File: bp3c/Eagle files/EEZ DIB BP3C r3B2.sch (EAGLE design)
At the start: 58 parts, among them IC1 TCA9534PWR, Q1 2N7002, Q2 2N7002, Q3 2N7002, Q4 2N7002, X1 ZL202-20G, X2 ZL202-20G, X3 ZL202-20G, X4 DS1022-2*20RF11, X5 DS1023-2*14S21, X6 DS1023-2*14S21, X7 DS1023-2*14S21, X8 N.C.

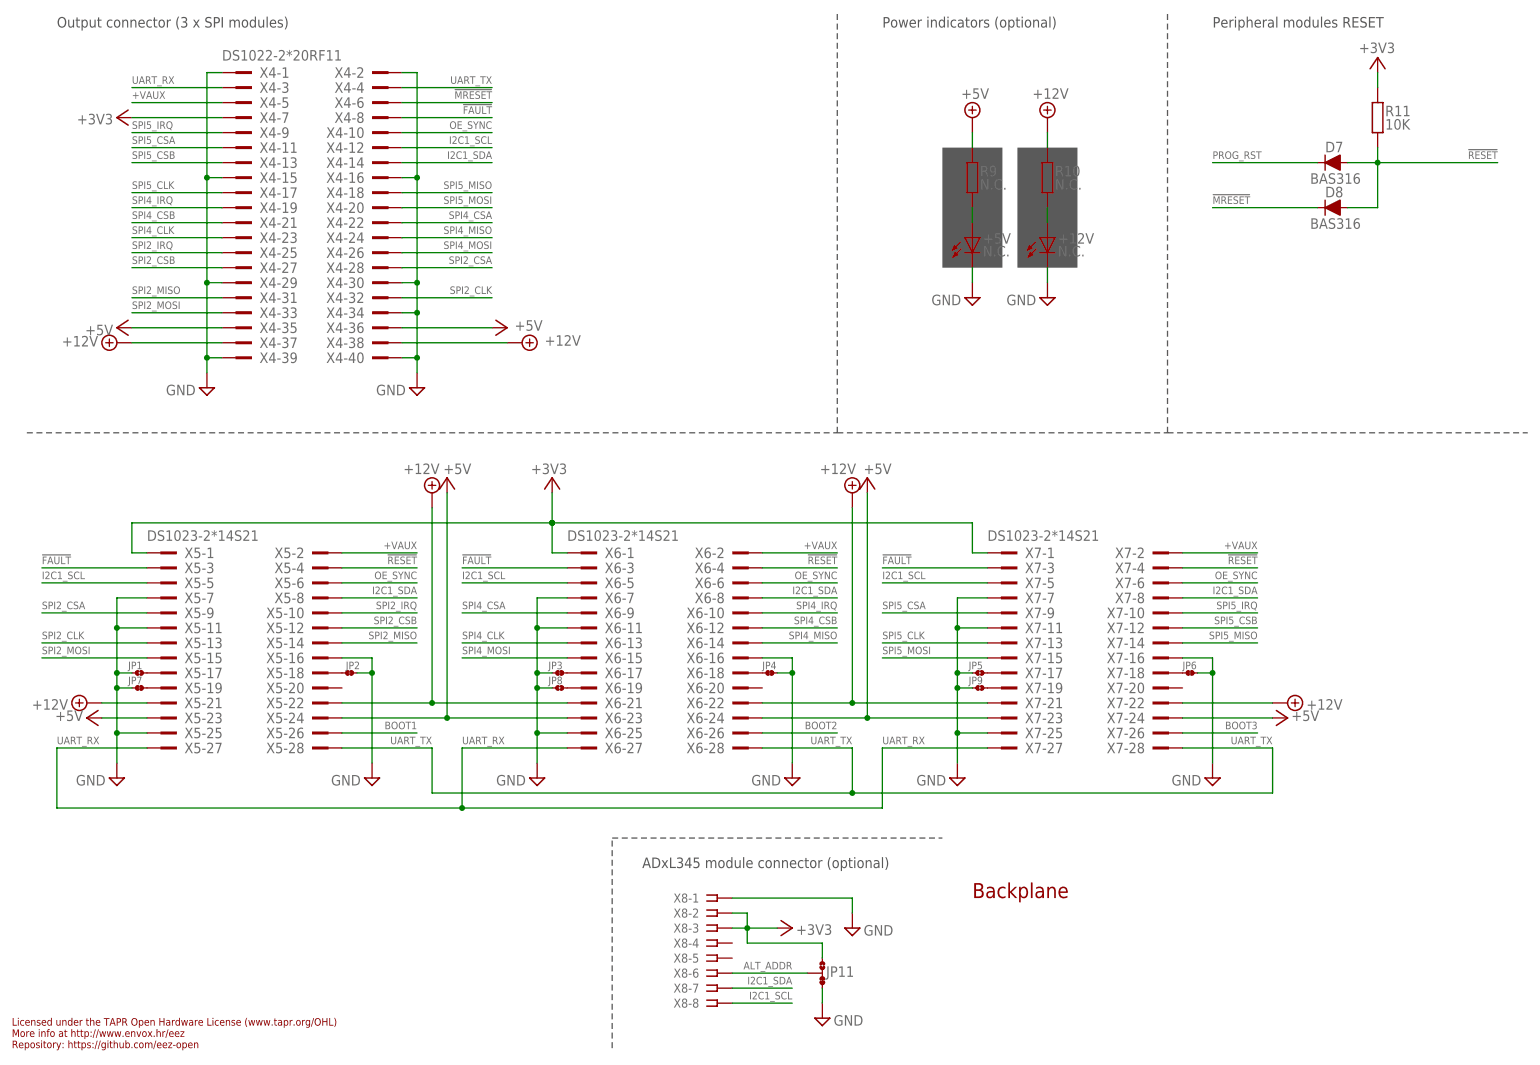
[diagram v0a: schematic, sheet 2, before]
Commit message: BP3C reset fix
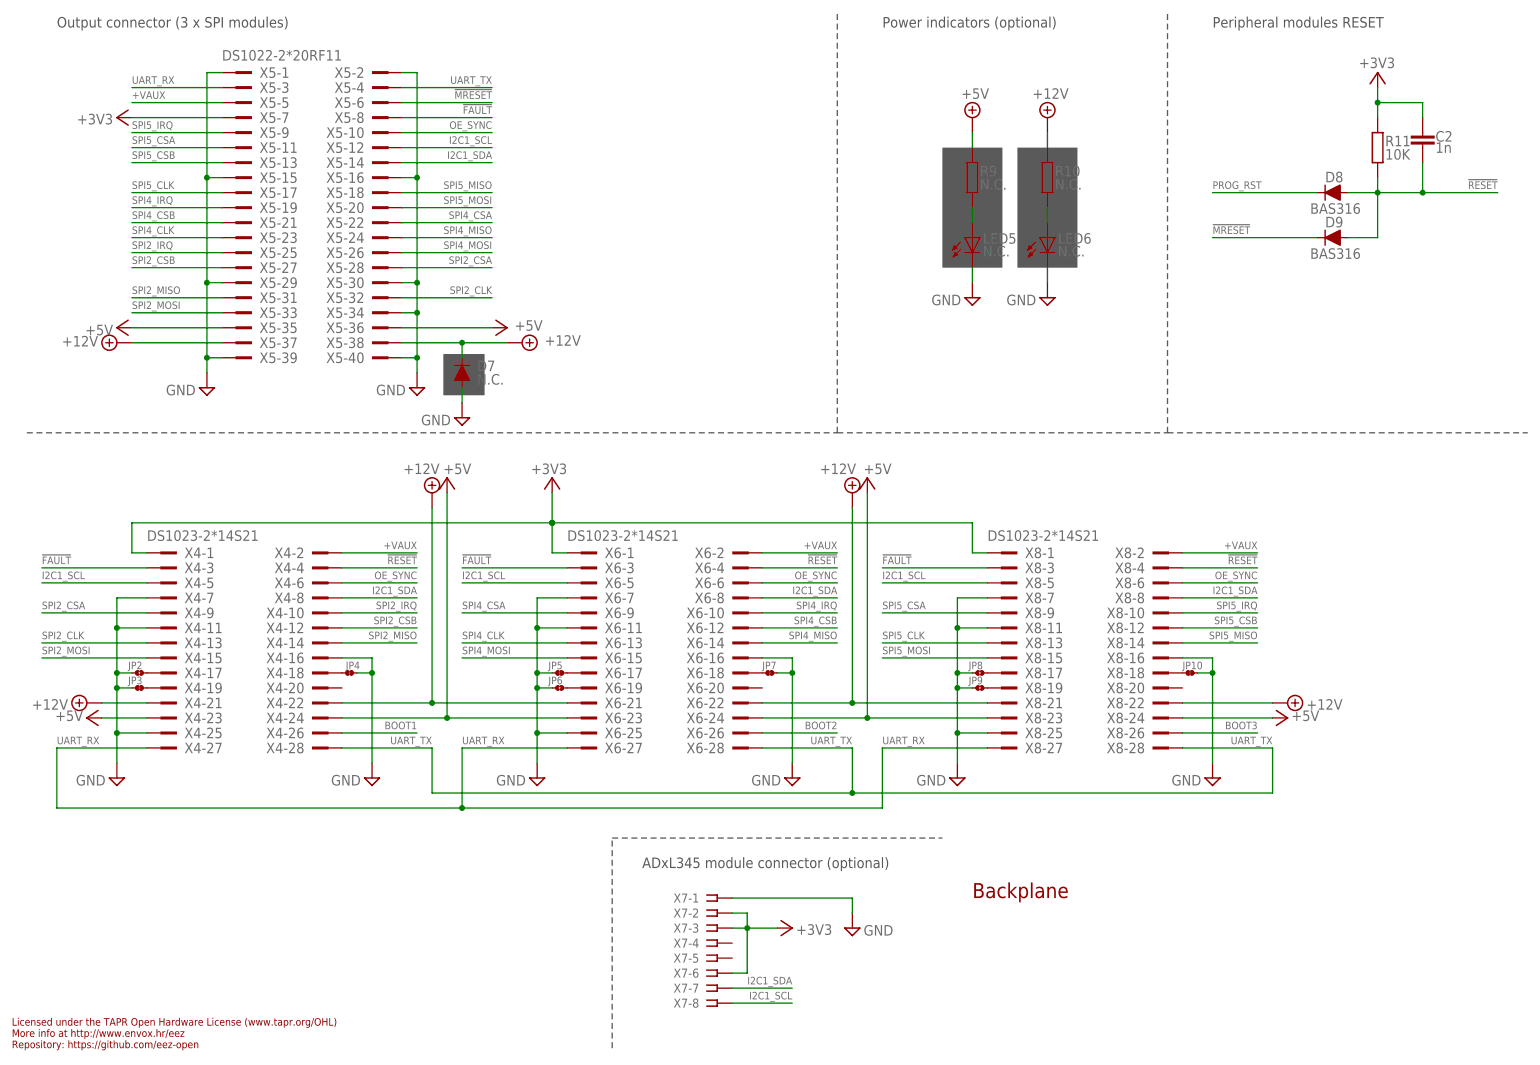
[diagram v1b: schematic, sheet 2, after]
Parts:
- removed JP11: JP3-CUT, EEZ_Lib1:JP3-CUT
- added C2: 1n, rcl:C-EUC0805
- added D9: BAS316, EEZ_Lib1:DIODESOD323R
- D1, D2: value BAS316 -> N.C.
- D3, D4: value N.C. -> BAS316
- D7: value BAS316 -> N.C.; device EEZ_Lib1:DIODESOD323R -> MyLib6:DIODEDO214AA
- JP1: value JP2-CUT -> JP3-CUT; device EEZ_Lib1:JP2-CUT -> EEZ_Lib1:JP3-CUT
- JP10: value JP3-CUT -> JP2-NOCUT; device EEZ_Lib1:JP3-CUT -> EEZ_Lib1:JP2-NOCUT
- JP2, JP6: value JP2-NOCUT -> JP2-CUT; device EEZ_Lib1:JP2-NOCUT -> EEZ_Lib1:JP2-CUT
- JP5: value JP2-CUT -> JP2-NOCUT; device EEZ_Lib1:JP2-CUT -> EEZ_Lib1:JP2-NOCUT
- R1, R5: value N.C. -> 100K
- R6, R8: value 100K -> N.C.
- X4: value DS1022-2*20RF11 -> DS1023-2*14S21; device EEZ_connectors:ZL212-40KG -> EEZ_connectors:TSW-114-07-F-D
- X5: value DS1023-2*14S21 -> DS1022-2*20RF11; device EEZ_connectors:TSW-114-07-F-D -> EEZ_connectors:ZL212-40KG
- X7: value DS1023-2*14S21 -> N.C.; device EEZ_connectors:TSW-114-07-F-D -> con-samtec:SSW-108-02-S-S
- X8: value N.C. -> DS1023-2*14S21; device con-samtec:SSW-108-02-S-S -> EEZ_connectors:TSW-114-07-F-D
- renumbered +12V to LED6, +5V to LED5, CGND to LED1, K_COMM to K3, K_PAR to K2, K_SER to K1, K_SRAIL to K4, PAR to LED2, SER to LED3, SRAIL to LED4
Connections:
- removed net ALT_ADDR: JP11.COM, X8-6.1
- removed net N$128 (its old number): D2.A, ZD2.A
- new net N$104: D4.A, ZD2.A
- net !FAULT: now also X4-3.1, X5-8.1, X8-3.1; no longer X4-8.1, X5-3.1, X7-3.1
- net !MRESET: now also D9.C, X5-6.1; no longer D8.C, X4-6.1
- net !RESET: now also C2.1, D9.A, X4-4.1, X8-4.1; no longer D7.A, X5-4.1, X7-4.1
- net +12V: now also D7.C, X4-21.1, X4-22.1, X5-37.1, X5-38.1, X8-21.1, X8-22.1; no longer X4-37.1, X4-38.1, X5-21.1, X5-22.1, X7-21.1, X7-22.1
- net +3V3: now also C2.2, JP1.NO, X4-1.1, X5-7.1, X7-2.1, X7-3.1, X7-6.1, X8-1.1; no longer JP10.NO, JP11.NO, X4-7.1, X5-1.1, X7-1.1, X8-2.1, X8-3.1
- net +5V: now also D3.C, D4.C, X4-23.1, X4-24.1, X5-35.1, X5-36.1, X8-23.1, X8-24.1; no longer D1.C, D2.C, X4-35.1, X4-36.1, X5-23.1, X5-24.1, X7-23.1, X7-24.1
- net +VAUX: now also X4-2.1, X5-5.1, X8-2.1; no longer X4-5.1, X5-2.1, X7-2.1
- net BOOT1: now also X4-26.1; no longer X5-26.1
- net BOOT3: now also X8-26.1; no longer X7-26.1
- net GND: now also D7.A, JP1.NC, JP10.2, JP2.1, JP6.1, JP7.2, R1.1, R5.1, X4-11.1, X4-25.1, X4-7.1, X5-1.1, X5-15.1, X5-2.1, X5-29.1, X5-30.1, X5-34.1, X5-39.1, X5-40.1, X7-1.1, X8-11.1, X8-16.1, X8-25.1, X8-7.1; no longer JP1.1, JP10.NC, JP11.NC, JP2.2, JP6.2, JP7.1, R6.1, R8.1, X4-1.1, X4-15.1, X4-2.1, X4-29.1, X4-30.1, X4-34.1, X4-39.1, X4-40.1, X5-11.1, X5-25.1, X5-7.1, X7-11.1, X7-16.1, X7-25.1, X7-7.1, X8-1.1
- net I2C1_SCL: now also X4-5.1, X5-12.1, X7-8.1, X8-5.1; no longer X4-12.1, X5-5.1, X7-5.1, X8-8.1
- net I2C1_SDA: now also X4-8.1, X5-14.1, X7-7.1, X8-8.1; no longer X4-14.1, X5-8.1, X7-8.1, X8-7.1
- net N$10: now also JP5.2; no longer JP3.2
- net N$101: now also Q2.D, R6.2, ZD2.C; no longer Q3.D, R5.2, ZD3.C
- net N$102: now also Q3.D, R7.2, ZD3.C; no longer Q2.D, R3.2, ZD2.C
- net N$11: now also JP6.2; no longer JP8.2
- net N$12: now also JP10.1, X8-18.1; no longer JP6.1, X7-18.1
- net N$13: now also JP8.2, X8-17.1; no longer JP5.2, X7-17.1
- net N$14: now also X8-19.1; no longer X7-19.1
- net N$15: now also JP1.COM; no longer JP10.COM
- net N$17: now also R3.2; no longer R1.2
- net N$18: now also D3.A; no longer D1.A
- net N$19: now also R3.1; no longer R1.1
- net N$2: now also JP4.1, X4-18.1; no longer JP2.1, X5-18.1
- net N$20: now also R8.2; no longer R7.2
- net N$22: now also R8.1; no longer R7.1
- net N$5: now also JP2.2, X4-17.1; no longer JP1.2, X5-17.1
- net N$6: now also JP3.2, X4-19.1; no longer JP7.2, X5-19.1
- net N$7: now also R6.1; no longer R5.1
- net N$8: now also R7.1; no longer R3.1
- net N$9: now also JP7.1; no longer JP4.1
- net OE_SYNC: now also X4-6.1, X5-10.1, X8-6.1; no longer X4-10.1, X5-6.1, X7-6.1
- net OUT_CGND: now also D1.C, R1.2; no longer D3.C, R2.2
- net OUT_PAR: now also D2.A, Q3.G; no longer D4.A, Q2.G
- net OUT_SER: now also D1.A, D2.C, Q2.G, R2.2; no longer D3.A, D4.C, Q3.G, R6.2
- net OUT_SRA: now also R5.2; no longer R8.2
- net PROG_RST: now also D8.C; no longer D7.C
- net SPI2_CLK: now also X4-13.1, X5-32.1; no longer X4-32.1, X5-13.1
- net SPI2_CSA: now also X4-9.1, X5-28.1; no longer X4-28.1, X5-9.1
- net SPI2_CSB: now also X4-12.1, X5-27.1; no longer X4-27.1, X5-12.1
- net SPI2_IRQ: now also X4-10.1, X5-25.1; no longer X4-25.1, X5-10.1
- net SPI2_MISO: now also X4-14.1, X5-31.1; no longer X4-31.1, X5-14.1
- net SPI2_MOSI: now also X4-15.1, X5-33.1; no longer X4-33.1, X5-15.1
- net SPI4_CLK: now also X5-23.1; no longer X4-23.1
- net SPI4_CSA: now also X5-22.1; no longer X4-22.1
- net SPI4_CSB: now also X5-21.1; no longer X4-21.1
- net SPI4_IRQ: now also X5-19.1; no longer X4-19.1
- net SPI4_MISO: now also X5-24.1; no longer X4-24.1
- net SPI4_MOSI: now also X5-26.1; no longer X4-26.1
- net SPI5_CLK: now also X5-17.1, X8-13.1; no longer X4-17.1, X7-13.1
- net SPI5_CSA: now also X5-11.1, X8-9.1; no longer X4-11.1, X7-9.1
- net SPI5_CSB: now also X5-13.1, X8-12.1; no longer X4-13.1, X7-12.1
- net SPI5_IRQ: now also X5-9.1, X8-10.1; no longer X4-9.1, X7-10.1
- net SPI5_MISO: now also X5-18.1, X8-14.1; no longer X4-18.1, X7-14.1
- net SPI5_MOSI: now also X5-20.1, X8-15.1; no longer X4-20.1, X7-15.1
- net UART_RX: now also X4-27.1, X5-3.1, X8-27.1; no longer X4-3.1, X5-27.1, X7-27.1
- net UART_TX: now also X4-28.1, X5-4.1, X8-28.1; no longer X4-4.1, X5-28.1, X7-28.1
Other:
- moved on the sheet: D1, D2, D3, D4, D5, D7, D8, JP3, JP4, JP7, JP8, Q2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

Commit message: add OSHWA ID on BP3C PCB
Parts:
- added OSHWA: HR000002, EEZ_Lib1:OSHWA-CERT-SMALL
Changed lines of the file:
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@@
 <setting verticaltext="up"/>
 </settings>
-<grid distance="0.1" unitdist="inch" unit="inch" style="lines" multiple="1" display="no" altdistance="0.01" altunitdist="inch" altunit="inch"/>
+<grid distance="0.025" unitdist="inch" unit="inch" style="lines" multiple="4" display="no" altdistance="0.01" altunitdist="inch" altunit="inch"/>
 <layers>
 <layer number="1" name="Top" color="4" fill="1" visible="no" active="no"/>
@@
 <part name="D7" library="MyLib6" deviceset="DIODE" device="DO214AA" value="N.C."/>
 <part name="SUPPLY14" library="supply2" deviceset="GND" device=""/>
+<part name="OSHWA" library="EEZ_Lib1" deviceset="OSHWA-CERT" device="-SMALL" value="HR000002"/>
 </parts>
 <sheets>
@@
 <attribute name="NAME" x="13.97" y="90.805" size="1.778" layer="95"/>
 </instance>
+<instance part="OSHWA" gate="G$1" x="8.255" y="11.43" smashed="yes">
+<attribute name="VALUE" x="2.286" y="8.89" size="1.778" layer="94" font="vector" ratio="12"/>
+</instance>
 </instances>

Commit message: Centroid files added
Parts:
- added FM1, FM2: FIDUCIAL, EEZ_Lib1:FIDUCIAL
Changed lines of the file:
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@@
 <setting verticaltext="up"/>
 </settings>
-<grid distance="0.025" unitdist="inch" unit="inch" style="lines" multiple="4" display="no" altdistance="0.01" altunitdist="inch" altunit="inch"/>
+<grid distance="0.1" unitdist="inch" unit="inch" style="lines" multiple="1" display="no" altdistance="0.01" altunitdist="inch" altunit="inch"/>
 <layers>
 <layer number="1" name="Top" color="4" fill="1" visible="no" active="no"/>
@@
 <part name="SUPPLY14" library="supply2" deviceset="GND" device=""/>
 <part name="OSHWA" library="EEZ_Lib1" deviceset="OSHWA-CERT" device="-SMALL" value="HR000002"/>
+<part name="FM1" library="EEZ_Lib1" deviceset="FIDUCIAL" device=""/>
+<part name="FM2" library="EEZ_Lib1" deviceset="FIDUCIAL" device=""/>
 </parts>
 <sheets>
@@
 <attribute name="VALUE" x="2.286" y="8.89" size="1.778" layer="94" font="vector" ratio="12"/>
 </instance>
+<instance part="FM1" gate="FD" x="149.86" y="5.08" smashed="yes"/>
+<instance part="FM2" gate="FD" x="157.48" y="5.08" smashed="yes"/>
 </instances>
 <busses>

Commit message: BP3C description fixed
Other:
- note added: "18 SPI5_MISO"
- note added: "20 SPI5_MOSI"
- note added: "22 SPI4_CSA"
- note added: "24 SPI4_MISO"
- note added: "26 SPI4_MOSI"
- note added: "28 SPI2_CSA"
- note added: "30 Gnd"
- note added: "32 SPI2_SCLK"
- note added: "SPI2_CSB 27"
- note added: "SPI2_IRQ 25"
- note added: "SPI2_MISO 31"
- note added: "SPI2_MOSI 33"
- note added: "SPI4_CSB 21"
- note added: "SPI4_IRQ 19"
- note added: "SPI4_SCLK 23"
- note added: "SPI5_CSA 11"
- note added: "SPI5_CSB 13"
- note added: "SPI5_IRQ 9"
- note added: "SPI5_SCLK 17"
- note removed: "16 GnD"
- note removed: "18 CH3_MISO"
- note removed: "20 CH3_MOSI"
- note removed: "22 CH2_CSA"
- note removed: "24 CH2_MISO"
- note removed: "26 CH2_MOSI"
- note removed: "28 Gnd"
- note removed: "30 SSDA"
- note removed: "32 CH1_SCLK"
- note removed: "CH1_CSB 27"
- note removed: "CH1_IRQ 25"
- note removed: "CH1_MISO 31"
- note removed: "CH1_MOSI 33"
- note removed: "CH2_CSB 21"
- note removed: "CH2_IRQ 19"
- note removed: "CH2_SCLK 23"
- note removed: "CH3_CSA 11"
- note removed: "CH3_CSB 13"
- note removed: "CH3_IRQ 9"
- note removed: "CH3_SCLK 17"
